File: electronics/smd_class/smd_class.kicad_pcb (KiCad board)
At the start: 2 copper layers, 30 x 30 mm, 17 parts, among them CON1 AVR-ISP-6, P1 Outline, P2 OSHW, SW1 SW_Push, U1 ATTINY85-20SU

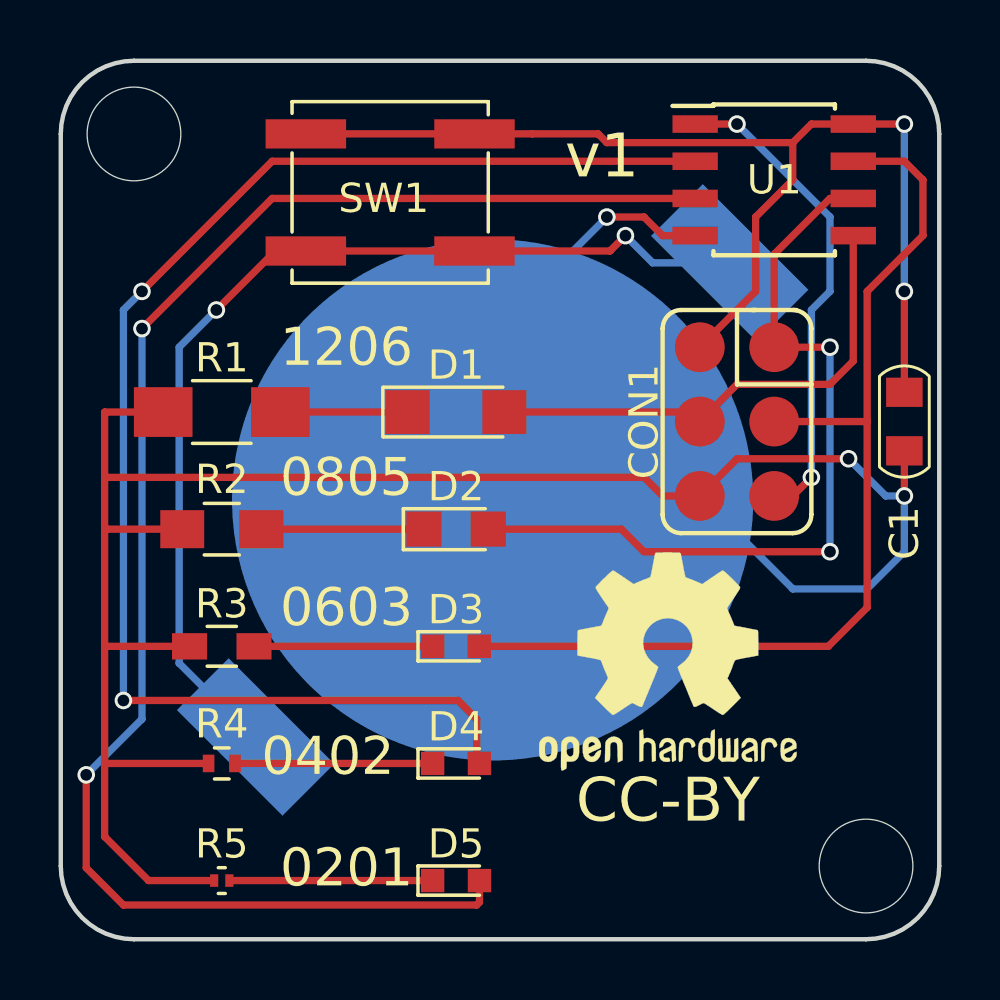
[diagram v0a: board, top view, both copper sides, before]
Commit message: smd_class: add ground pour, full url silk
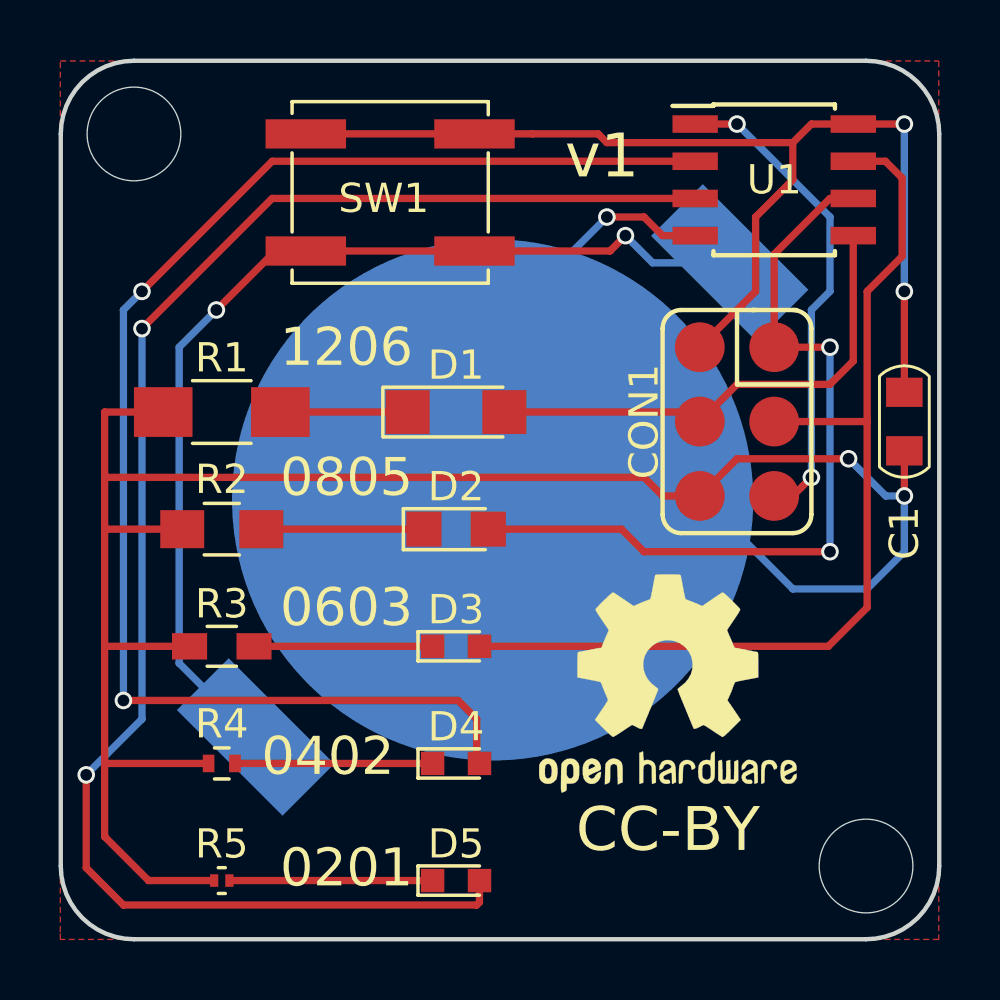
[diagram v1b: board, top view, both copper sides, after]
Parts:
- moved P2 0.75 mm to (169.2, 126.3)
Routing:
- net /SCK: track 35.0 -> 34.0 mm
- added copper zone on F.Cu, net GND
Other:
- board text added: "(c) Google, Inc"
- board text added: "electronics/smd_class"
- board text added: "github.com/google/"
- board text added: "makerspace-partsbin/"
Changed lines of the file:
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@@
     (area 147.899999 103.0286 179.100001 135.600001)
     (thickness 1.6)
-    (drawings 9)
+    (drawings 13)
     (tracks 124)
     (zones 0)
@@
     (34 B.Paste user)
     (35 F.Paste user)
-    (36 B.SilkS user hide)
+    (36 B.SilkS user)
     (37 F.SilkS user)
     (38 B.Mask user)
@@
     (last_trace_width 0.25)
     (trace_clearance 0.2)
-    (zone_clearance 0.508)
-    (zone_45_only no)
+    (zone_clearance 0.254)
+    (zone_45_only yes)
     (trace_min 0.2)
     (segment_width 0.2)
@@
   )
   (module Symbols:OSHW-Logo2_9.8x8mm_SilkScreen (layer F.Cu)
-    (at 169.235 125.51)
+    (at 169.235 126.26)
     (descr "Open Source Hardware Symbol")
     (tags "Logo Symbol OSHW")
@@
       (net 1 "Net-(BT1-Pad1)"))
   )
-  (gr_text CC-BY (at 169.235 130.26) (layer F.SilkS)
+  (gr_text "(c) Google, Inc" (at 163.485 107.76 180) (layer B.SilkS)
+    (effects (font (size 1.3 1.3) (thickness 0.3)) (justify mirror))
+  )
+  (gr_text electronics/smd_class (at 176.485 118.26 270) (layer B.SilkS)
+    (effects (font (size 1.3 1.3) (thickness 0.3)) (justify mirror))
+  )
+  (gr_text makerspace-partsbin/ (at 161.485 132.76 180) (layer B.SilkS)
+    (effects (font (size 1.3 1.3) (thickness 0.3)) (justify mirror))
+  )
+  (gr_text github.com/google/ (at 150.485 121.76 90) (layer B.SilkS)
+    (effects (font (size 1.3 1.3) (thickness 0.3)) (justify mirror))
+  )
+  (gr_text CC-BY (at 169.235 131.26) (layer F.SilkS)
     (effects (font (size 1.5 1.5) (thickness 0.3)))
   )
@@
   (segment (start 163.5 121) (end 163.1 121) (width 0.25) (layer F.Cu) (net 6))
   (segment (start 160.9 121) (end 155.35 121) (width 0.25) (layer F.Cu) (net 7))
+  (segment (start 177.235 109.01) (end 176.66 108.435) (width 0.25) (layer F.Cu) (net 8))
+  (segment (start 176.66 108.435) (end 175.565 108.435) (width 0.25) (layer F.Cu) (net 8) (status 800000))
+  (segment (start 177.235 111.685) (end 177.235 109.01) (width 0.25) (layer F.Cu) (net 8))
+  (segment (start 176.04 112.88) (end 177.235 111.685) (width 0.25) (layer F.Cu) (net 8))
   (segment (start 176.04 117.325) (end 176.04 112.88) (width 0.25) (layer F.Cu) (net 8))
-  (segment (start 176.04 112.88) (end 177.945 110.975) (width 0.25) (layer F.Cu) (net 8))
   (segment (start 162.8 125) (end 174.715 125) (width 0.25) (layer F.Cu) (net 8))
   (segment (start 176.04 123.675) (end 176.04 117.325) (width 0.25) (layer F.Cu) (net 8))
   (segment (start 174.715 125) (end 176.04 123.675) (width 0.25) (layer F.Cu) (net 8))
   (segment (start 172.865 117.325) (end 176.04 117.325) (width 0.25) (layer F.Cu) (net 8))
-  (segment (start 177.31 108.435) (end 175.565 108.435) (width 0.25) (layer F.Cu) (net 8))
-  (segment (start 177.945 109.07) (end 177.31 108.435) (width 0.25) (layer F.Cu) (net 8))
-  (segment (start 177.945 110.975) (end 177.945 109.07) (width 0.25) (layer F.Cu) (net 8))
   (segment (start 161.2 125) (end 155.1 125) (width 0.25) (layer F.Cu) (net 9))
   (segment (start 170.165 108.435) (end 155.72 108.435) (width 0.25) (layer F.Cu) (net 10))
@@
   (via (at 171.595 107.165) (size 0.6) (drill 0.4) (layers F.Cu B.Cu) (net 14))
   (segment (start 171.595 107.165) (end 170.165 107.165) (width 0.25) (layer F.Cu) (net 14))
+  (zone (net 2) (net_name GND) (layer F.Cu) (hatch edge 0.508)
+    (connect_pads (clearance 0.254))
+    (min_thickness 0.254)
+    (fill yes (arc_segments 16) (thermal_gap 0.508) (thermal_bridge_width 0.508))
+    (polygon
+      (pts
+        (xy 148.485 105.01) (xy 178.485 105.01) (xy 178.485 135.01) (xy 148.485 135.01) (xy 148.485 134.76)
+      )
+    )
+  )
 )
